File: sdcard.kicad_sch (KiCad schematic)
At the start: 4 parts, among them J12 Micro_SD_Card_Det, U19 RT9742GGJ5

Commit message: [WIP] PCB commit
Signed-off-by: Dominik Sliwa <dominik@sliwa.io>
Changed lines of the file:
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@@
     (in_bom yes) (on_board yes)
     (property "Reference" "R36" (id 0) (at 66.675 85.725 90))
-    (property "Value" "10k" (id 1) (at 70.485 85.725 90))
+    (property "Value" "10k" (id 1) (at 71.755 85.725 90))
     (property "Footprint" "Resistor_SMD:R_0402_1005Metric" (id 2) (at 69.215 83.185 0)
       (effects (font (size 1.27 1.27)) hide)

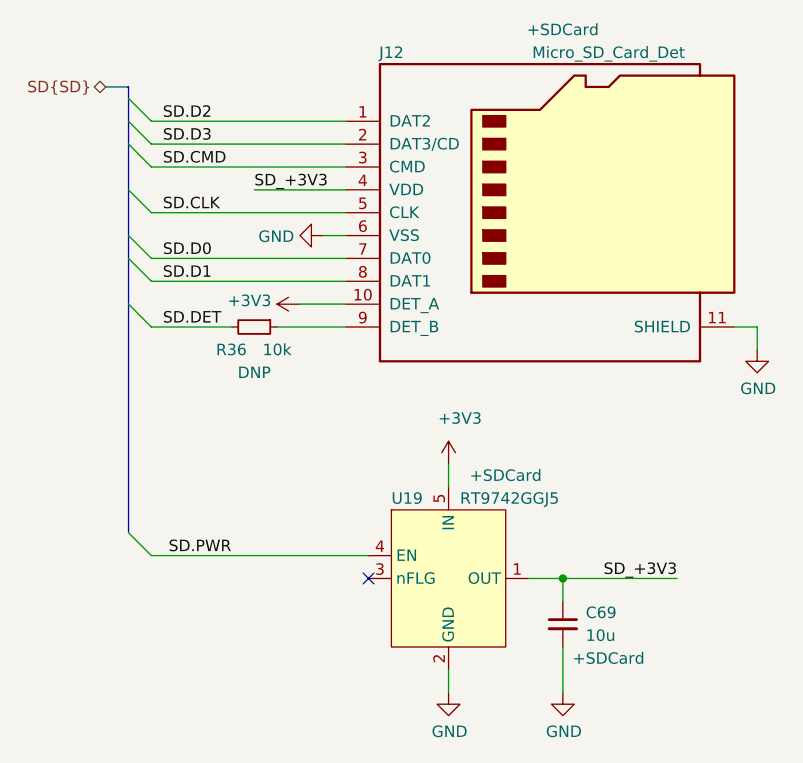
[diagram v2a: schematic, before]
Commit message: sdcard.kicad_sch: add 10k pull-up on SD.PWR
During boot process cm4 puts that pin briefly in input mode.

Signed-off-by: Dominik Sliwa <dominik@sliwa.io>
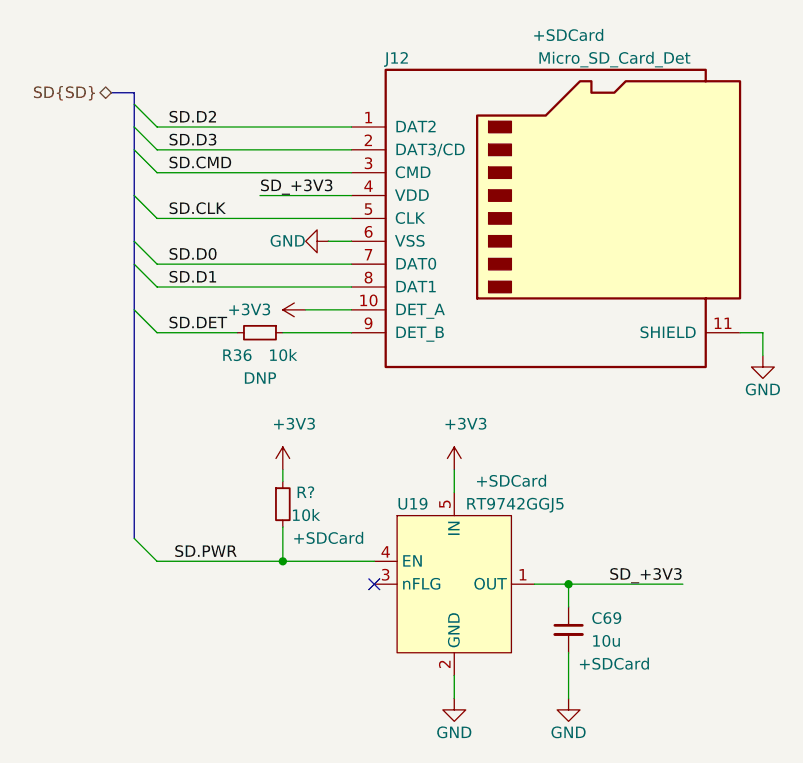
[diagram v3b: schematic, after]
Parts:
- added R?: 10k, Resistor_SMD:R_0402_1005Metric, symbol Device:R_Small
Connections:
- net +3V3: now also R?.1
- net SD.PWR: now also R?.2
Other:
- moved on the sheet: C69, J12, R36, U19

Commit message: Assign footprints and annotate components
Signed-off-by: Stefan Agner <stefan@agner.ch>
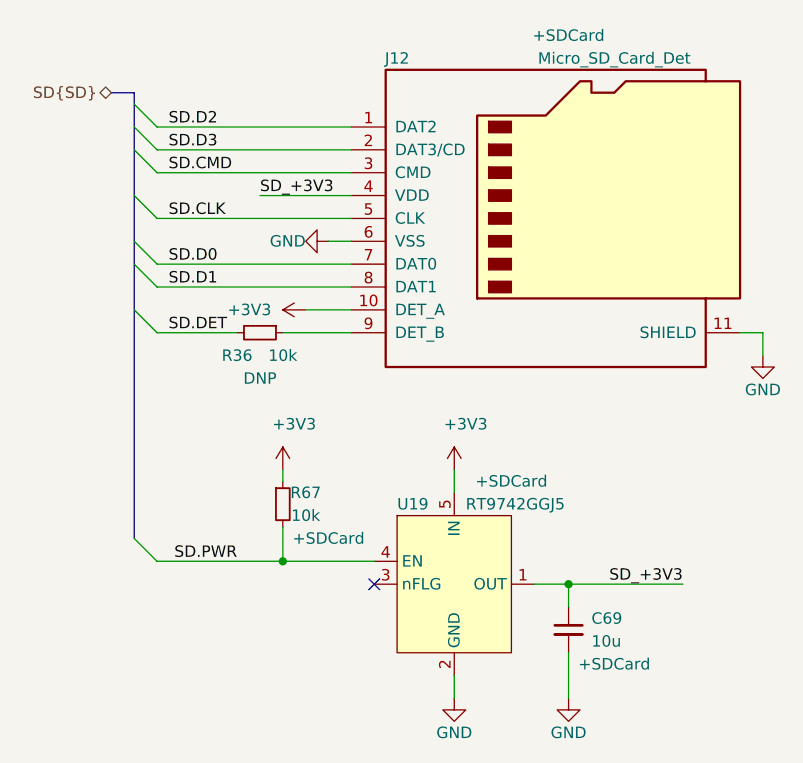
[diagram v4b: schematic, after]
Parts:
- gave numbers to parts that had none: 1
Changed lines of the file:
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@@
-(kicad_sch (version 20210126) (generator eeschema)
+(kicad_sch (version 20210406) (generator eeschema)
   (paper "A4")
   (title_block
@@
     (stroke (width 0) (type solid) (color 0 0 0 0))
   )
-  (bus (pts (xy 55.88 57.15) (xy 55.88 58.42))
-    (stroke (width 0) (type solid) (color 0 0 0 0))
-  )
-  (bus (pts (xy 55.88 58.42) (xy 55.88 60.96))
-    (stroke (width 0) (type solid) (color 0 0 0 0))
-  )
-  (bus (pts (xy 55.88 63.5) (xy 55.88 60.96))
-    (stroke (width 0) (type solid) (color 0 0 0 0))
-  )
-  (bus (pts (xy 55.88 63.5) (xy 55.88 68.58))
-    (stroke (width 0) (type solid) (color 0 0 0 0))
-  )
-  (bus (pts (xy 55.88 68.58) (xy 55.88 73.66))
-    (stroke (width 0) (type solid) (color 0 0 0 0))
-  )
-  (bus (pts (xy 55.88 76.2) (xy 55.88 73.66))
-    (stroke (width 0) (type solid) (color 0 0 0 0))
-  )
-  (bus (pts (xy 55.88 76.2) (xy 55.88 81.28))
-    (stroke (width 0) (type solid) (color 0 0 0 0))
-  )
-  (bus (pts (xy 55.88 81.28) (xy 55.88 106.68))
+  (bus (pts (xy 55.88 57.15) (xy 55.88 106.68))
     (stroke (width 0) (type solid) (color 0 0 0 0))
   )
@@
   (symbol (lib_id "power:+3V3") (at 72.39 99.06 0) (unit 1)
     (in_bom yes) (on_board yes)
-    (property "Reference" "#PWR?" (id 0) (at 72.39 102.87 0)
+    (property "Reference" "#PWR0288" (id 0) (at 72.39 102.87 0)
       (effects (font (size 1.27 1.27)) hide)
     )
@@
   (symbol (lib_id "Device:R_Small") (at 72.39 102.87 0) (unit 1)
     (in_bom yes) (on_board yes)
-    (property "Reference" "R?" (id 0) (at 74.93 101.6 0))
+    (property "Reference" "R67" (id 0) (at 74.93 101.6 0))
     (property "Value" "10k" (id 1) (at 74.93 104.14 0))
     (property "Footprint" "Resistor_SMD:R_0402_1005Metric" (id 2) (at 72.39 102.87 0)
